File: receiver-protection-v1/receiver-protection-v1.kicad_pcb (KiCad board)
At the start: 2 copper layers, 61 x 29.2 mm, 13 parts, among them J1 INPUT, J2 OUTPUT, J3 POWER/CTRL, K1 DS1E-M-DC12V, Q1 2N3904

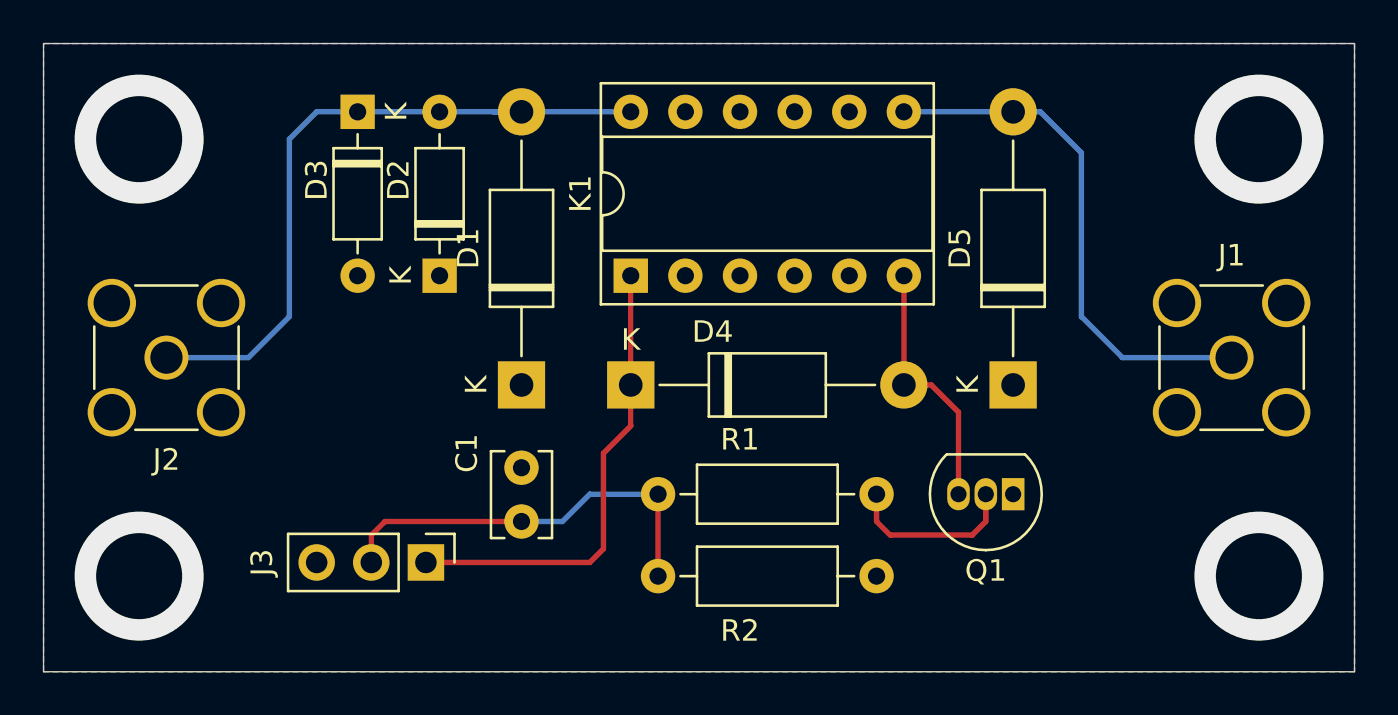
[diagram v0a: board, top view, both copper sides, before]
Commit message: add revision 1.1 changes
* make sure the mounting hole vias are attached to ground!
* reverse input/output - make sure that the SDR facing output
  has the protection diodes and optional surge protector, and
  is grounded when the enable signal isn't applied
* label input, output, power/ground/enable
* add description, my name, and revision number
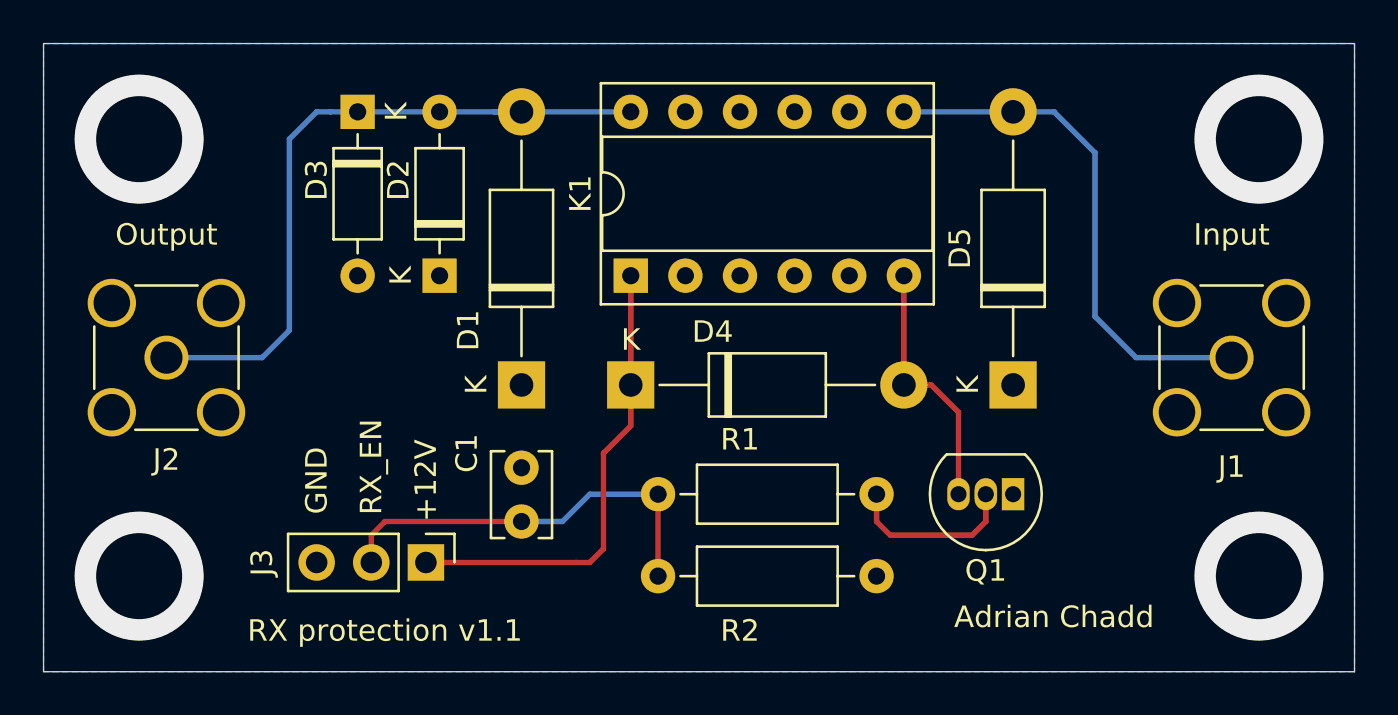
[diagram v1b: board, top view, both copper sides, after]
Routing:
- net GND: vias 0 -> 4
- net (no net): vias 4 -> 0
- removed copper zone on F.Cu, net GND
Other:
- board text added: "+12V"
- board text added: "Adrian Chadd"
- board text added: "GND"
- board text added: "Input"
- board text added: "Output"
- board text added: "RX protection v1.1"
- board text added: "RX_EN"
